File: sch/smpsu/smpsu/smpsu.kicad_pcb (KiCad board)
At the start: 2 copper layers, 88.9 x 69.9 mm, 50 parts, among them J1 Conn_01x01_Female, J10 Conn_01x01_Female, J11 Conn_01x01_Female, J12 Conn_01x01_Female, J13 Conn_01x01_Female, J14 Conn_01x01_Female, J15 Conn_01x01_Female, J16 Conn_01x01_Female, J17 Conn_01x01_Female, J2 Conn_01x01_Female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

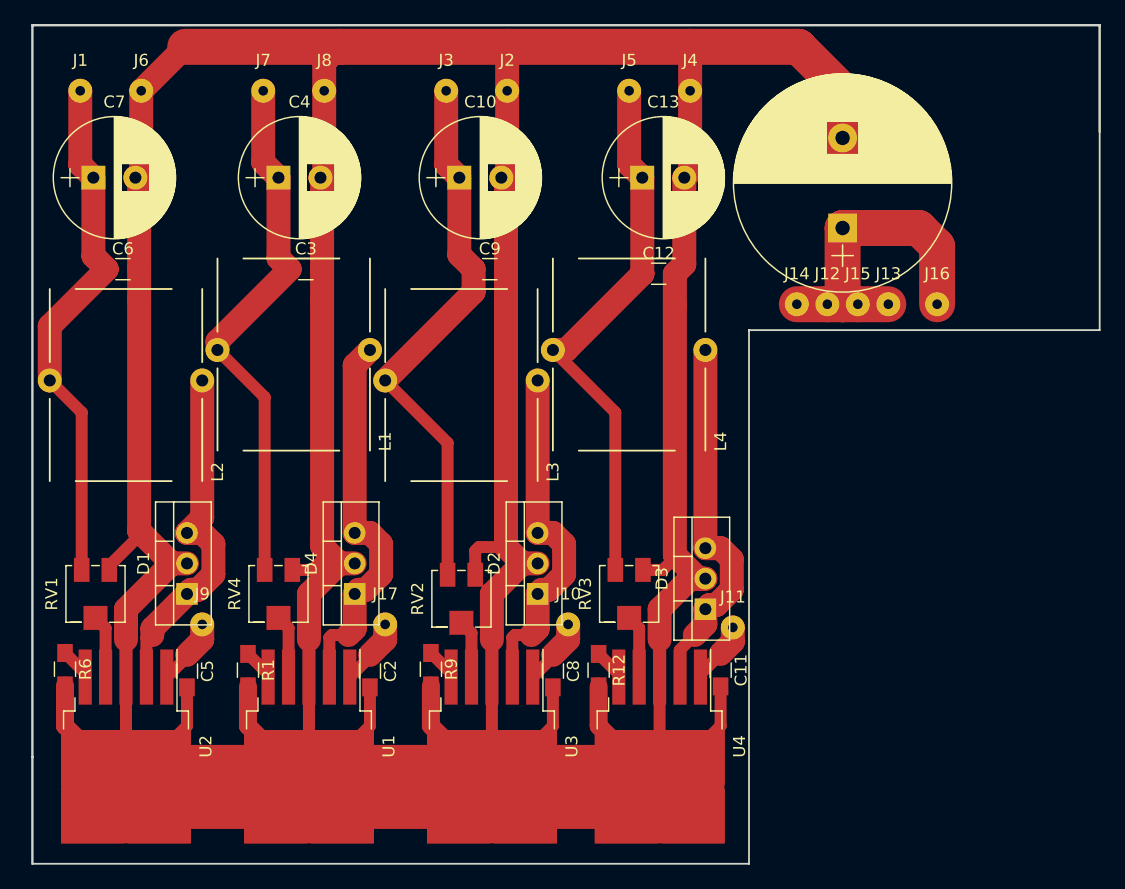
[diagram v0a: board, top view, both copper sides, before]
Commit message: Added smpsu test schematic and gerbers
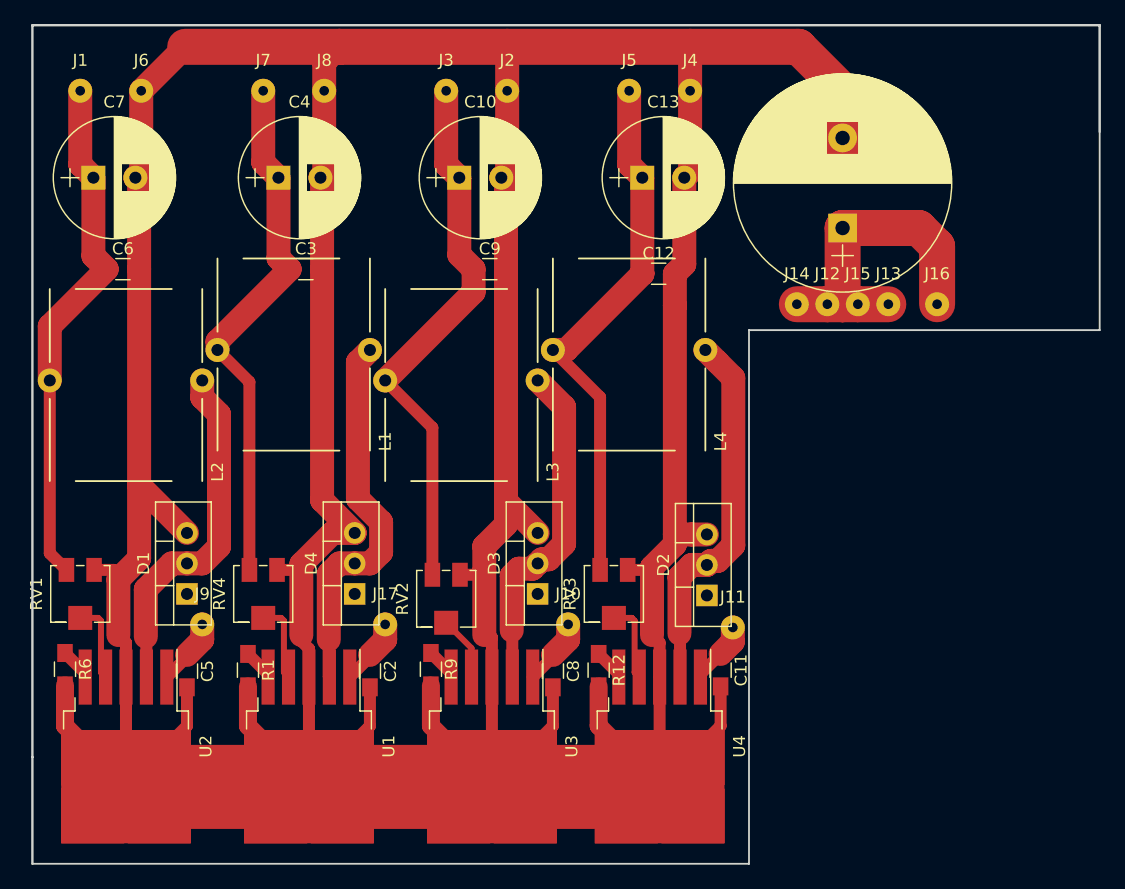
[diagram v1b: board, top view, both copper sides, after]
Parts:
- D1, D2, D3, D4: value D_Schottky_KAK -> D_Schottky_AKA
- moved D2 14.1 mm to (137.3, 114.4)
- moved D3 14.0 mm to (123.2, 114.3)
- moved RV2 1.27 mm to (115.6, 114.7)
- moved RV3 1.27 mm to (129.5, 114.3)
- moved RV1 1.27 mm to (85.1, 114.3)
- moved RV4 1.27 mm to (100.3, 114.3)
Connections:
- D1 pad 2: GND -> Net-(D1-Pad2)
- D1 pad 3: Net-(D1-Pad1) -> GND
- D2 pad 2: GND -> Net-(D2-Pad2)
- D2 pad 3: Net-(D2-Pad1) -> GND
- D3 pad 2: GND -> Net-(D3-Pad2)
- D3 pad 3: Net-(D3-Pad1) -> GND
- D4 pad 2: GND -> Net-(D4-Pad2)
- D4 pad 3: Net-(D4-Pad1) -> GND
- L1 pad 2: Net-(D4-Pad1) -> Net-(D4-Pad2)
- L2 pad 2: Net-(D1-Pad1) -> Net-(D1-Pad2)
- L3 pad 2: Net-(D2-Pad1) -> Net-(D3-Pad2)
- L4 pad 2: Net-(D3-Pad1) -> Net-(D2-Pad2)
- U1 pad 2: Net-(D4-Pad1) -> Net-(D4-Pad2)
- U2 pad 2: Net-(D1-Pad1) -> Net-(D1-Pad2)
- U3 pad 2: Net-(D2-Pad1) -> Net-(D3-Pad2)
- U4 pad 2: Net-(D3-Pad1) -> Net-(D2-Pad2)
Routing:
- net Net-(D4-Pad1): track 32.4 -> 0.00 mm
- net Net-(D4-Pad2): track 0.00 -> 31.8 mm
- net Net-(D2-Pad2): track 0.00 -> 31.2 mm
- net Net-(D3-Pad1): track 31.0 -> 0.00 mm
- net Net-(D1-Pad1): track 29.7 -> 0.00 mm
- net Net-(D1-Pad2): track 0.00 -> 29.3 mm
- net Net-(D2-Pad1): track 29.3 -> 0.00 mm
- net Net-(D3-Pad2): track 0.00 -> 28.4 mm
- net Net-(RV3-Pad2): track 5.27 -> 6.68 mm
- net Net-(RV4-Pad2): track 5.27 -> 6.68 mm
- net Net-(RV1-Pad2): track 5.27 -> 6.68 mm
- net GND: track 468.2 -> 467.2 mm
- net Net-(RV2-Pad2): track 4.87 -> 5.39 mm
- net Net-(C12-Pad1): track 46.3 -> 45.7 mm
- net Net-(C10-Pad1): track 46.5 -> 45.9 mm
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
